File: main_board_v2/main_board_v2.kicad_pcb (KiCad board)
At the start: 2 copper layers, 100 x 274 mm, 66 parts, among them J1 Raspberry_Pi_4, U1 4N35, U2 Pico, U3 Pico

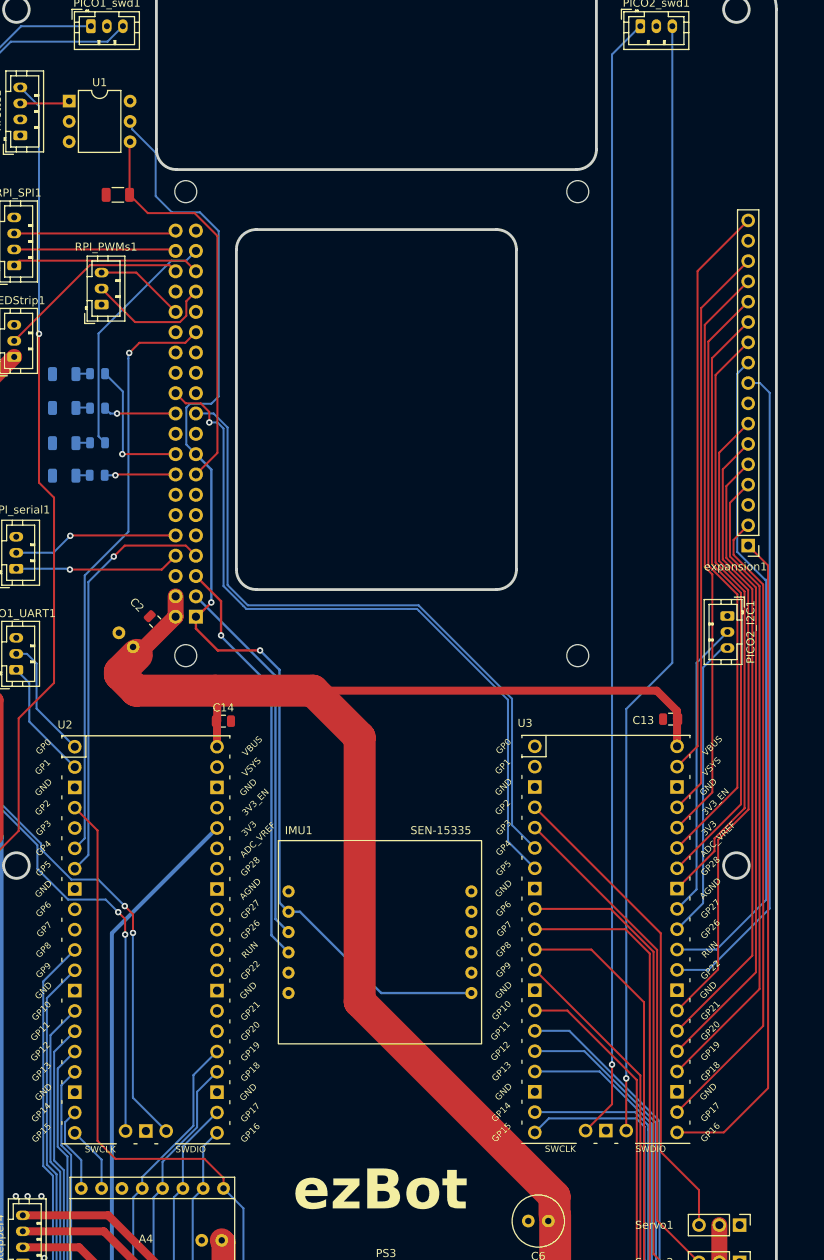
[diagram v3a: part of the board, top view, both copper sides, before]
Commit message: Added plug for raspberry switches and corrected all DRCs
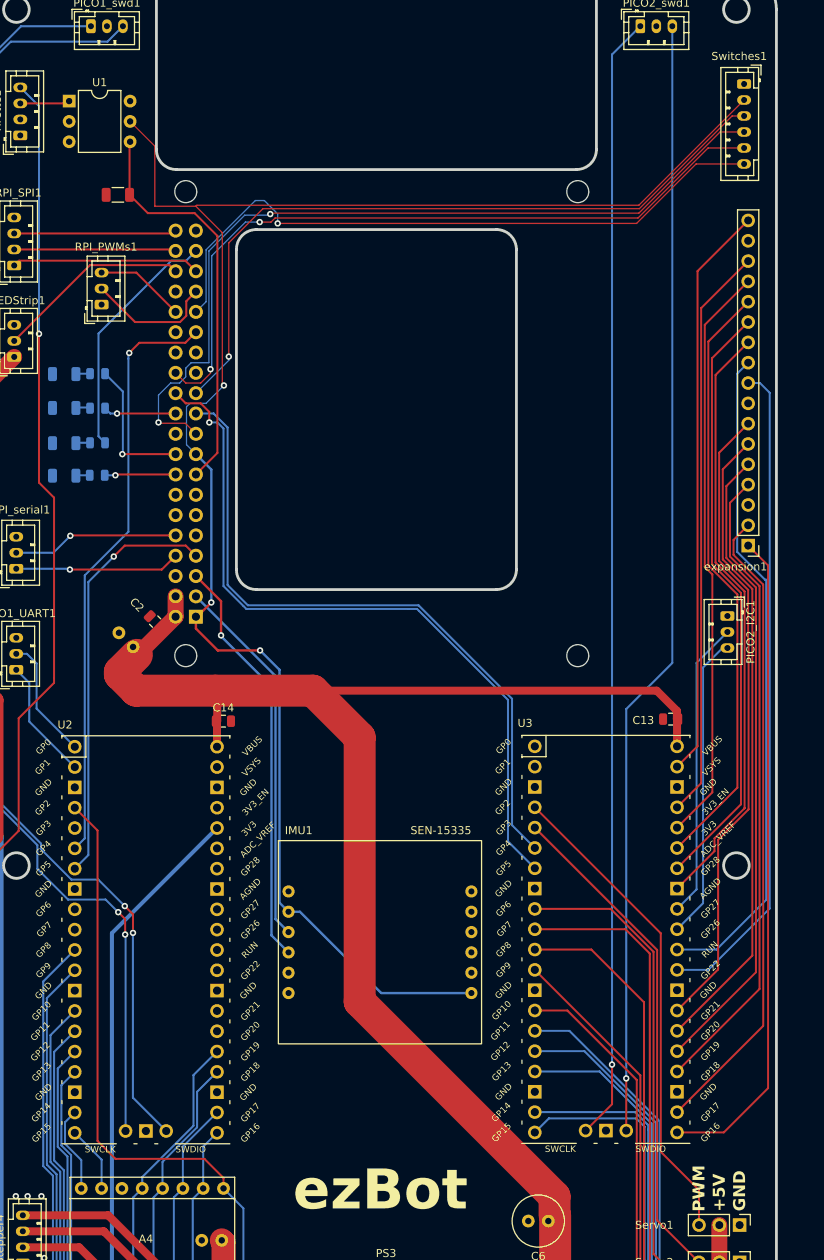
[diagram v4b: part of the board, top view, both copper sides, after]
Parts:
- added Switches1: Conn_01x06_Pin, Connector_JST:JST_PH_B6B-PH-K_1x06_P2.00mm_Vertical, F.Cu at (340.9, 61.3)
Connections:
- J1 pad 19: unconnected-(J1-MOSI0/GPIO10-Pad19) -> Net-(J1-MOSI0/GPIO10)
- J1 pad 23: unconnected-(J1-SCLK0/GPIO11-Pad23) -> Net-(J1-SCLK0/GPIO11)
- J1 pad 26: unconnected-(J1-~{CE1}/GPIO7-Pad26) -> Net-(J1-~{CE1}/GPIO7)
- J1 pad 31: unconnected-(J1-GCLK2/GPIO6-Pad31) -> Net-(J1-GCLK2/GPIO6)
- Servo10 pad 3: /servo7 -> /servo9
- Servo11 pad 3: /servo9 -> /servo10
- Servo2 pad 3: /servo2 -> /servo1
- Servo3 pad 3: /servo4 -> /servo2
- Servo4 pad 2: +7.5V -> +5VP
- Servo4 pad 3: /servo6 -> /servo3
- Servo5 pad 2: +7.5V -> +5VP
- Servo5 pad 3: /servo8 -> /servo4
- Servo6 pad 2: +7.5V -> +5VP
- Servo6 pad 3: /servo10 -> /servo5
- Servo7 pad 2: +5VP -> +7.5V
- Servo7 pad 3: /servo1 -> /servo6
- Servo8 pad 2: +5VP -> +7.5V
- Servo8 pad 3: /servo3 -> /servo7
- Servo9 pad 2: +5VP -> +7.5V
- Servo9 pad 3: /servo5 -> /servo8
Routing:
- net Net-(J1-MOSI0/GPIO10): track 0.00 -> 104.3 mm, vias 0 -> 2
- net Net-(J1-~{CE1}/GPIO7): track 0.00 -> 92.3 mm, vias 0 -> 2
- net Net-(J1-SCLK0/GPIO11): track 0.00 -> 91.5 mm, vias 0 -> 1
- net Net-(J1-GCLK2/GPIO6): track 0.00 -> 83.0 mm, vias 0 -> 1
- net +3.3V: track 145.5 -> 220.9 mm, vias 2 -> 3
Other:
- board text added: "+5V"
- board text added: "GND"
- board text added: "PWM"
